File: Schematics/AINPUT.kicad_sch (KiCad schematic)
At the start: 3 parts, among them J3 AudioJack2_Switch, J4 AudioJack2_Switch, U2 Opamp_Dual

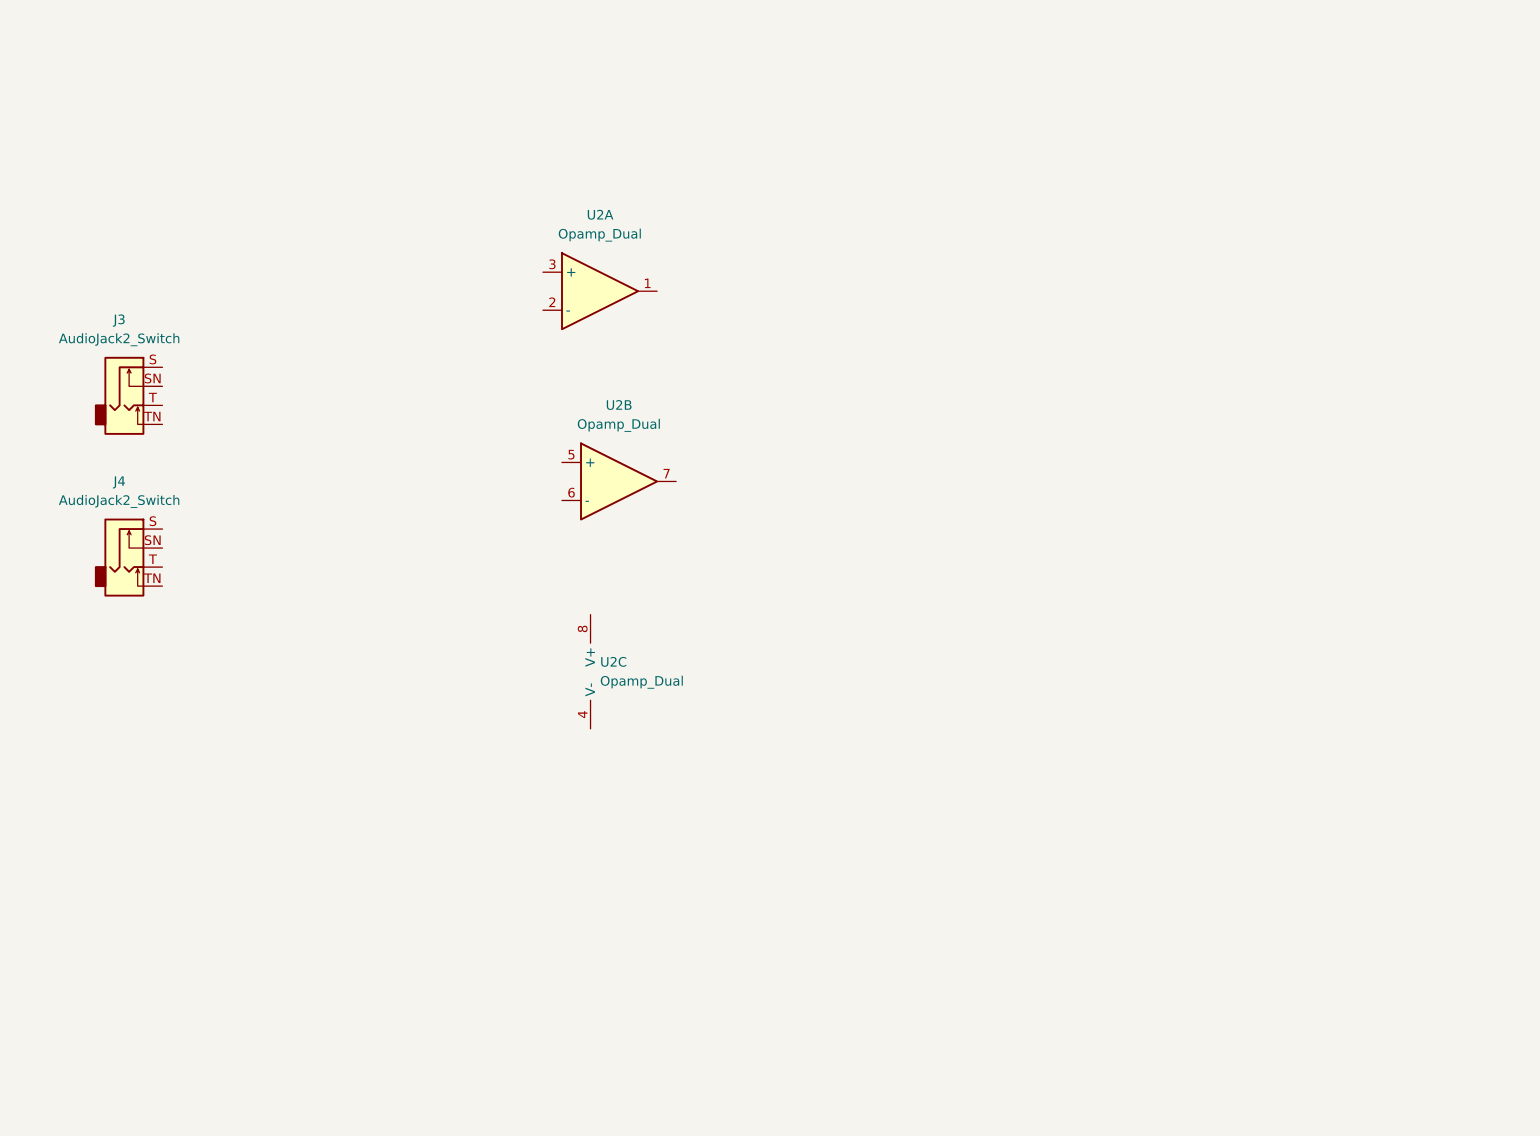
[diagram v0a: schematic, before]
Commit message: Added recommended op-amps
Added recommended op-amps (without values) with dual mono TS in and out
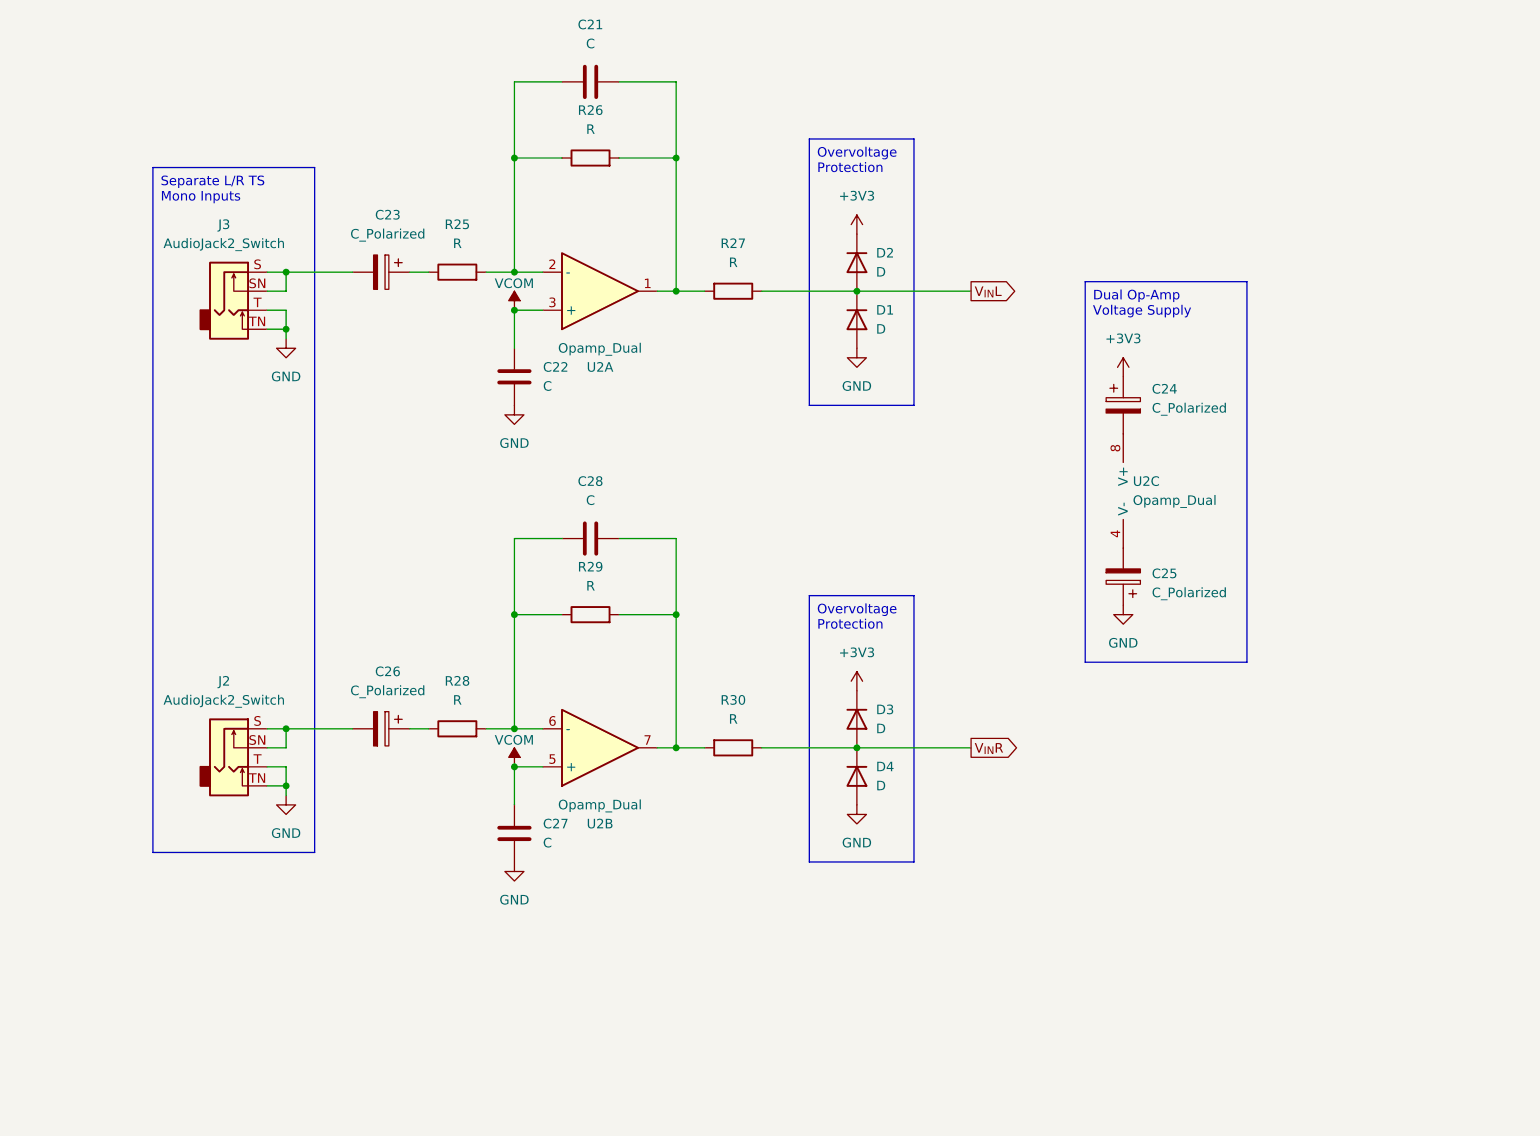
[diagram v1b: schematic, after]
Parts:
- removed J4: AudioJack2_Switch, symbol Connector_Audio:AudioJack2_Switch
- added C21, C22, C27, C28: C, symbol Device:C
- added C23, C24, C25, C26: C_Polarized, symbol Device:C_Polarized
- added D1, D2, D3, D4: D, symbol Device:D
- added J2: AudioJack2_Switch, symbol Connector_Audio:AudioJack2_Switch
- added R25, R26, R27, R28, R29, R30: R, symbol Device:R
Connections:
- net VCOM: now reaches U2.5 (+)
- net VCOM: now also U2.3 (+), C22.1, C27.1
- net at U2.6 (-): now also C28.1, R28.2, R29.1
- net at U2.7: now also C28.2, R29.2, R30.2
- net at U2.4 (V-): now also C25.2
- net at U2.8 (V+): now also C24.2
- net at J3.S: now also J3.SN, C23.2
- net GND: now reaches J3.T
- net GND: now also J3.TN, C22.2, C25.1, C27.2, D1.2 (A), D4.2 (A), J2.T, J2.TN
- net at U2.1: now also C21.2, R26.2, R27.2
- net at U2.2 (-): now also C21.1, R25.2, R26.1
- new net: C23.1, R25.1
- new net: C26.1, R28.1
- new net: C26.2, J2.S, J2.SN
- new net +3V3: C24.1, D2.1 (K), D3.1 (K)
- new net V_{IN}L: D1.1 (K), D2.2 (A), R27.1
- new net V_{IN}R: D3.2 (A), D4.1 (K), R30.1
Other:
- moved on the sheet: J3, U2B, U2C

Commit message: Input Buffer & EEPROM
line and instrument level buffers for the input added. EEPROM added and credits attributed !
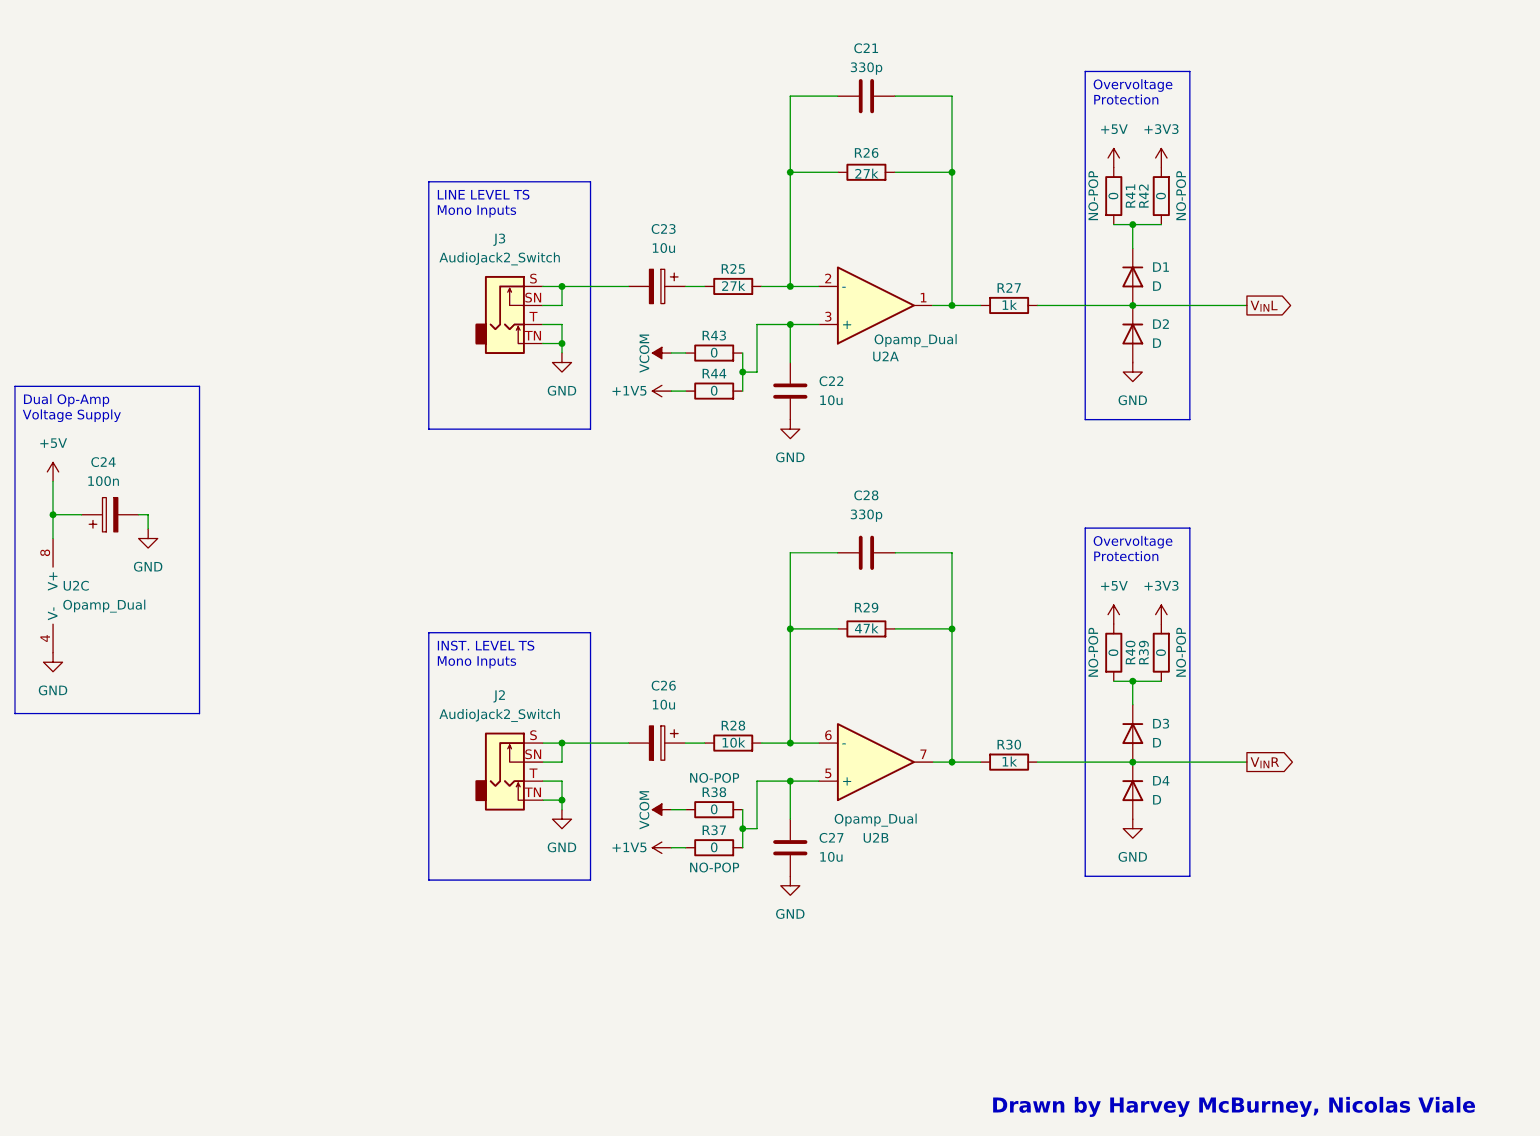
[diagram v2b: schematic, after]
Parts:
- removed C25: C_Polarized, symbol Device:C_Polarized
- added R37, R38, R39, R40, R41, R42, R43, R44: 0, symbol Device:R
- C21, C28: value C -> 330p
- C22, C27: value C -> 10u
- C23, C26: value C_Polarized -> 10u
- C24: value C_Polarized -> 100n
- R25, R26: value R -> 27k
- R27, R30: value R -> 1k
- R28: value R -> 10k
- R29: value R -> 47k
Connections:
- net +3V3: now also R39.2, R42.2; no longer C24.1, D2.1 (K), D3.1 (K)
- net GND: now also C24.2, D2.2 (A), U2.4 (V-); no longer D1.2 (A)
- net VCOM: now also R38.1, R43.1; no longer C22.1, C27.1, U2.3 (+), U2.5 (+)
- net V_{IN}L: now also D1.2 (A), D2.1 (K); no longer D1.1 (K), D2.2 (A)
- net +5V: now reaches U2.8 (V+)
- net +5V: now also C24.1, R40.1, R41.1; no longer C24.2
- new net: D1.1 (K), R41.2, R42.1
- new net: C27.1, R37.2, R38.2, U2.5 (+)
- new net: C22.1, R43.2, R44.2, U2.3 (+)
- new net: D3.1 (K), R39.1, R40.2
- new net +1V5: R37.1, R44.1
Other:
- note added: "Drawn by Harvey McBurney, Nicolas Viale"
- title: (none) -> Audio Input Buffer
- moved on the sheet: C21, C22, C23, C26, C27, C28, D3, D4, J2, J3, R25, R26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
